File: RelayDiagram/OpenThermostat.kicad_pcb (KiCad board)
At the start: 2 copper layers, 88 parts, among them J1 Conn_01x08_Female, J2 Conn_01x15_Female, J3 Conn_01x15_Female, J4 Conn_01x09_Female, Q1 Q_NMOS_DGS, Q10 Q_NMOS_DGS, Q11 Q_NMOS_DGS, Q12 Q_NMOS_DGS, Q2 Q_NMOS_DGS, Q3 Q_NMOS_DGS, Q4 Q_NMOS_DGS, Q5 Q_NMOS_DGS, Q6 Q_NMOS_DGS, Q7 Q_NMOS_DGS, Q8 Q_NMOS_DGS, Q9 Q_NMOS_DGS, SW2 SW_Push, SW3 SW_Push, SW4 SW_Push, SW5 SW_Push, SW6 SW_Push, U1 PCF8574, U2 LCD, U3 DHT11, U4 EE2-3TNU-L_DPDT_Relay, U5 EE2-3TNU-L_DPDT_Relay, U6 EE2-3TNU-L_DPDT_Relay, U7 EE2-3TNU-L_DPDT_Relay, U8 EE2-3TNU-L_DPDT_Relay, U9 EE2-3TNU-L_DPDT_Relay

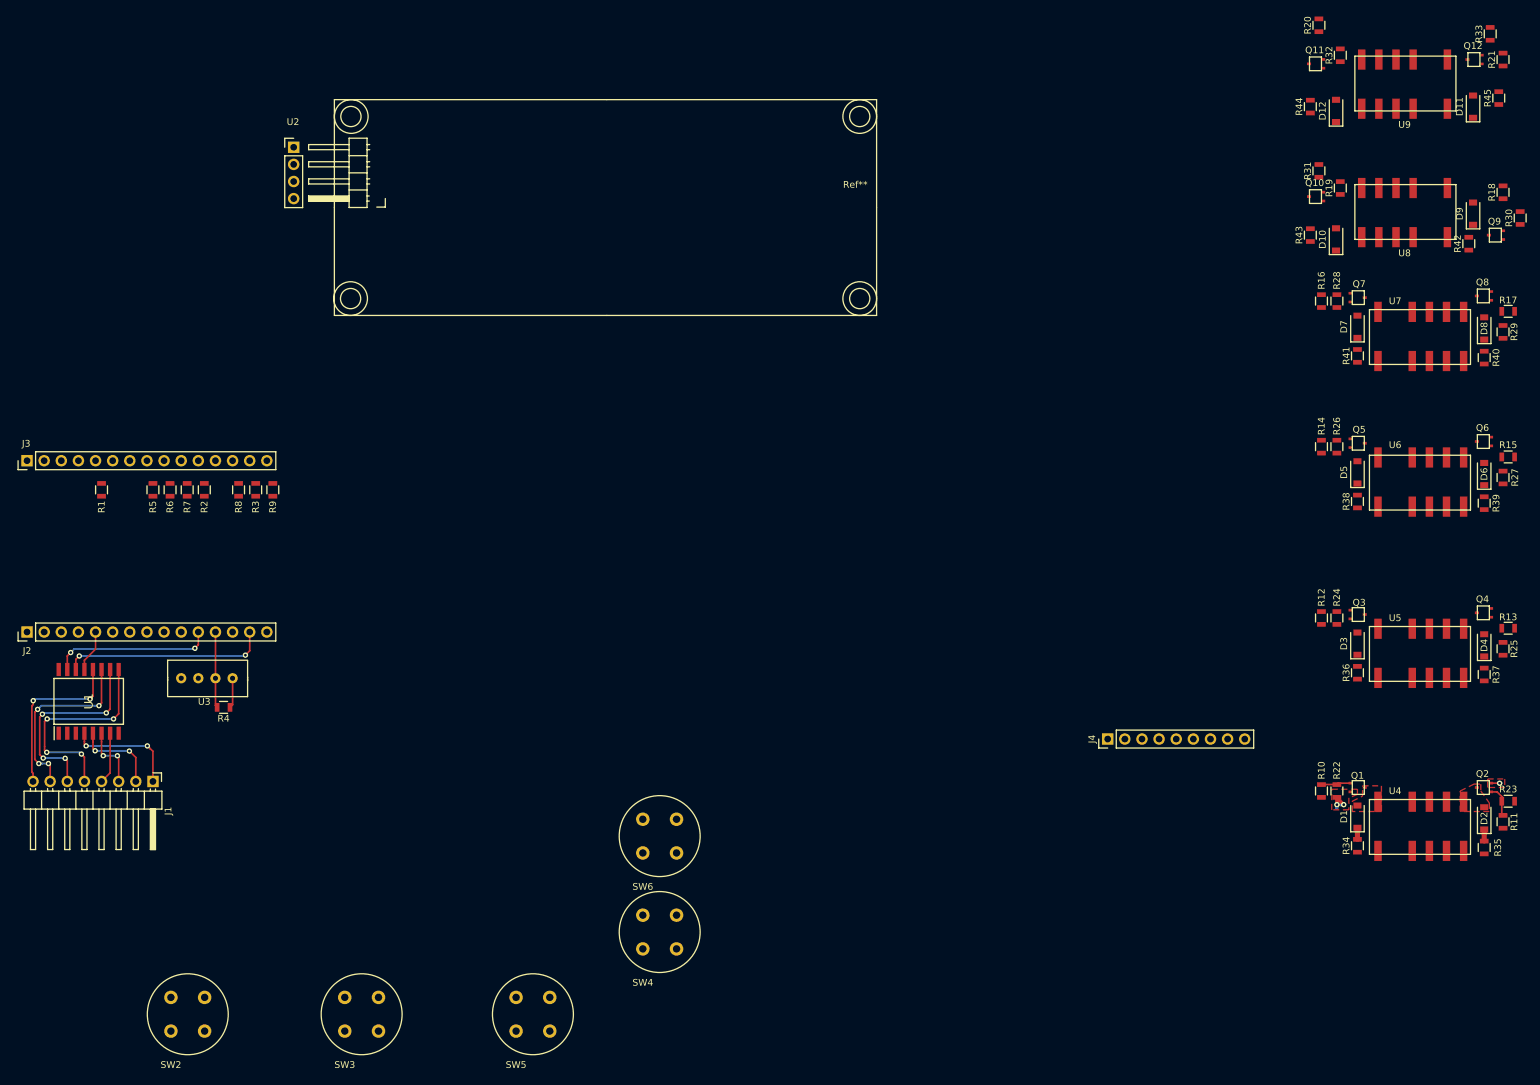
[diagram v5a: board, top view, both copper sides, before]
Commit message: Routed LCD and placed buttons. Added edges to board, but it will most likely need to be extended to route the relays
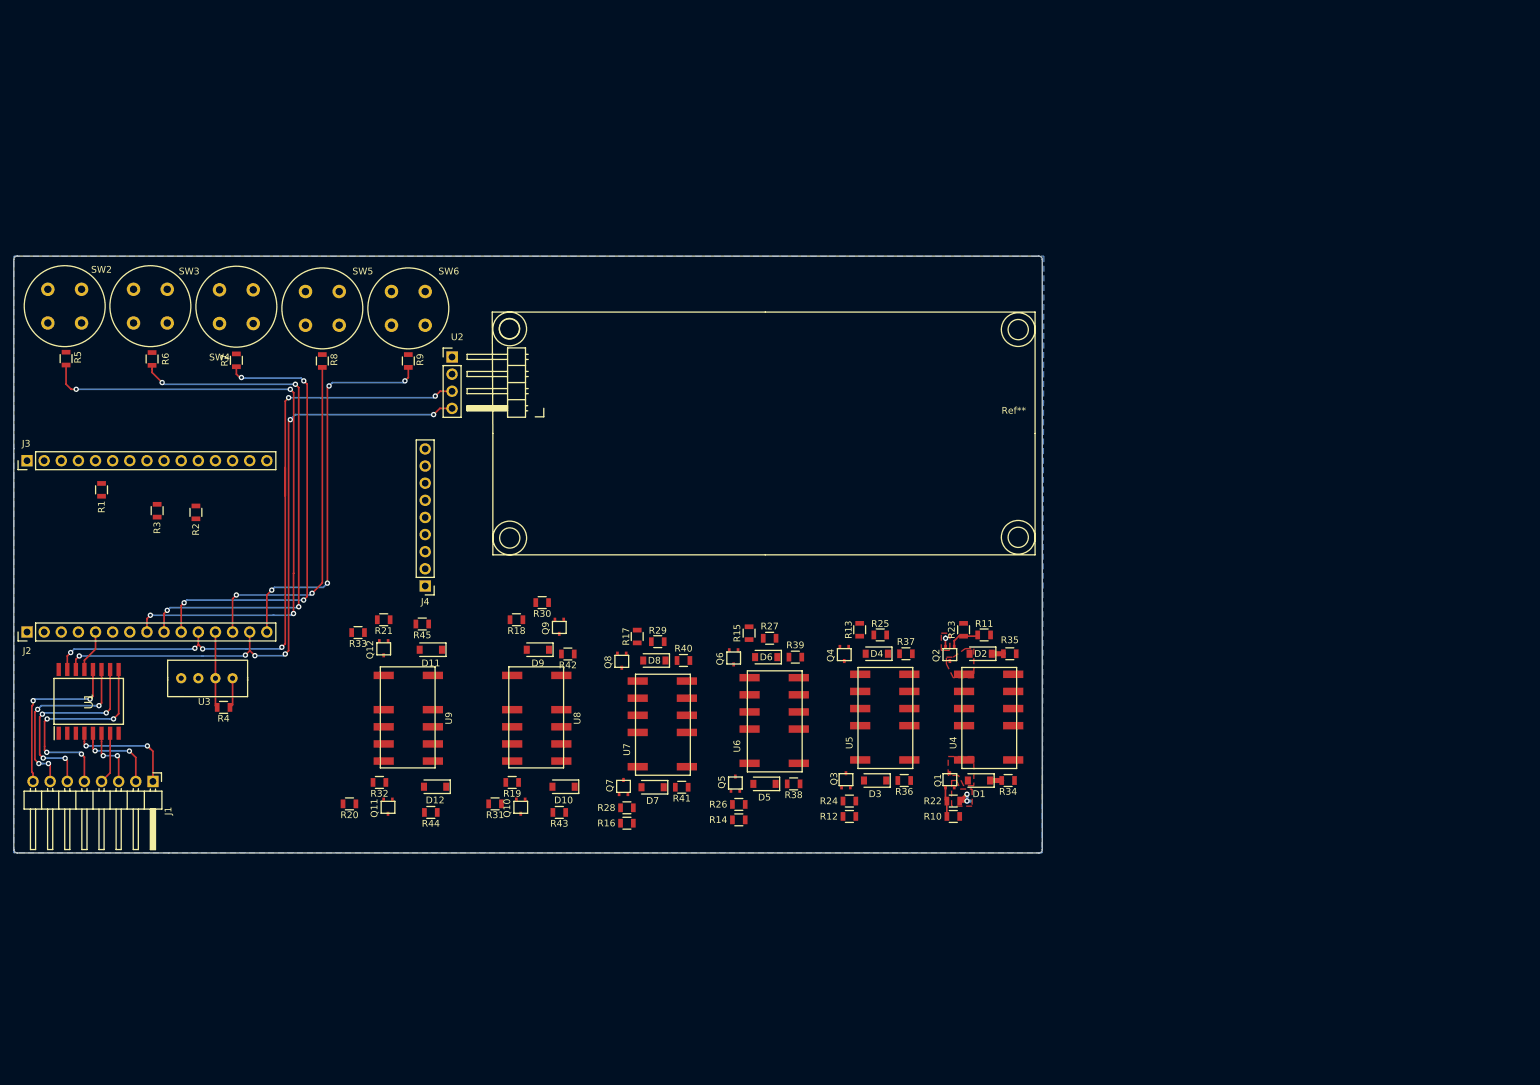
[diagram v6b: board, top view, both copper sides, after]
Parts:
- moved R33 189.9 mm to (102.0, 126.3), turned to 180 degrees
- moved R21 185.6 mm to (105.9, 124.4), turned to 180 degrees
- moved R20 184.4 mm to (100.8, 151.7), turned to 180 degrees
- moved Q12 184.2 mm to (105.9, 127.6), turned to 180 degrees
- moved U9 182.3 mm to (105.9, 132.7), turned to 270 degrees
- moved R32 178.7 mm to (105.2, 148.5), turned to 180 degrees
- moved R45 177.7 mm to (111.6, 125.1), turned to 180 degrees
- moved Q11 176.4 mm to (106.5, 151.1), turned to 180 degrees
- moved D11 174.3 mm to (112.8, 128.9), turned to 180 degrees
- moved R44 167.2 mm to (112.8, 153.0), turned to 180 degrees
- moved D12 167.0 mm to (113.5, 149.2), turned to 180 degrees
- moved R18 159.4 mm to (125.5, 124.4), turned to 180 degrees
- moved U8 156.4 mm to (124.9, 132.7), turned to 270 degrees
- moved R30 155.8 mm to (129.3, 121.9), turned to 180 degrees
- moved R31 154.1 mm to (122.4, 151.7), turned to 180 degrees
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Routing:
- net Net-(J2-Pad8): track 0.00 -> 93.9 mm, vias 0 -> 4
- net Net-(J2-Pad9): track 0.00 -> 79.4 mm, vias 0 -> 4
- net Net-(J2-Pad11): track 24.0 -> 103.1 mm, vias 2 -> 6
- net Net-(J2-Pad10): track 0.00 -> 66.8 mm, vias 0 -> 4
- net Net-(J2-Pad14): track 30.6 -> 96.3 mm, vias 2 -> 6
- net Net-(J2-Pad15): track 0.00 -> 58.3 mm, vias 0 -> 4
- net Net-(J2-Pad13): track 0.00 -> 51.2 mm, vias 0 -> 2
- added copper zone on B.Cu, net GND
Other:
- board outline added: 152.5 x 88.5 mm

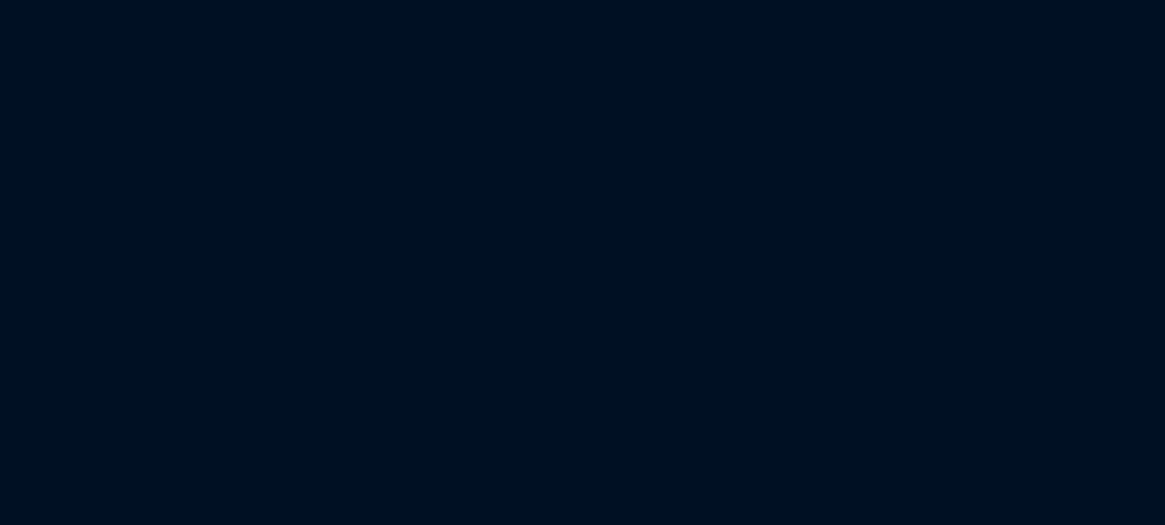
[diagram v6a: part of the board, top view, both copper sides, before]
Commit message: Added Power Components to schematic, Added Footprints
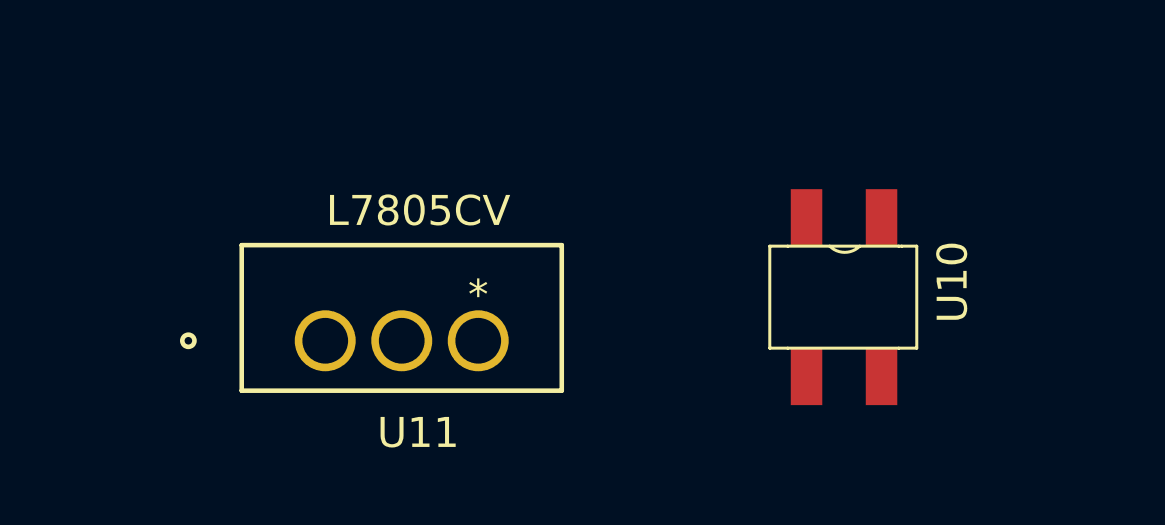
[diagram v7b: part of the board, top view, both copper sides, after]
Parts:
- added U10: MB10S-13, Open_Thermostat:MB10F-13, F.Cu at (137.7, 172.7)
- added U11: L7805CV, Open_Thermostat:L7805CV, F.Cu at (127.2, 169.1)

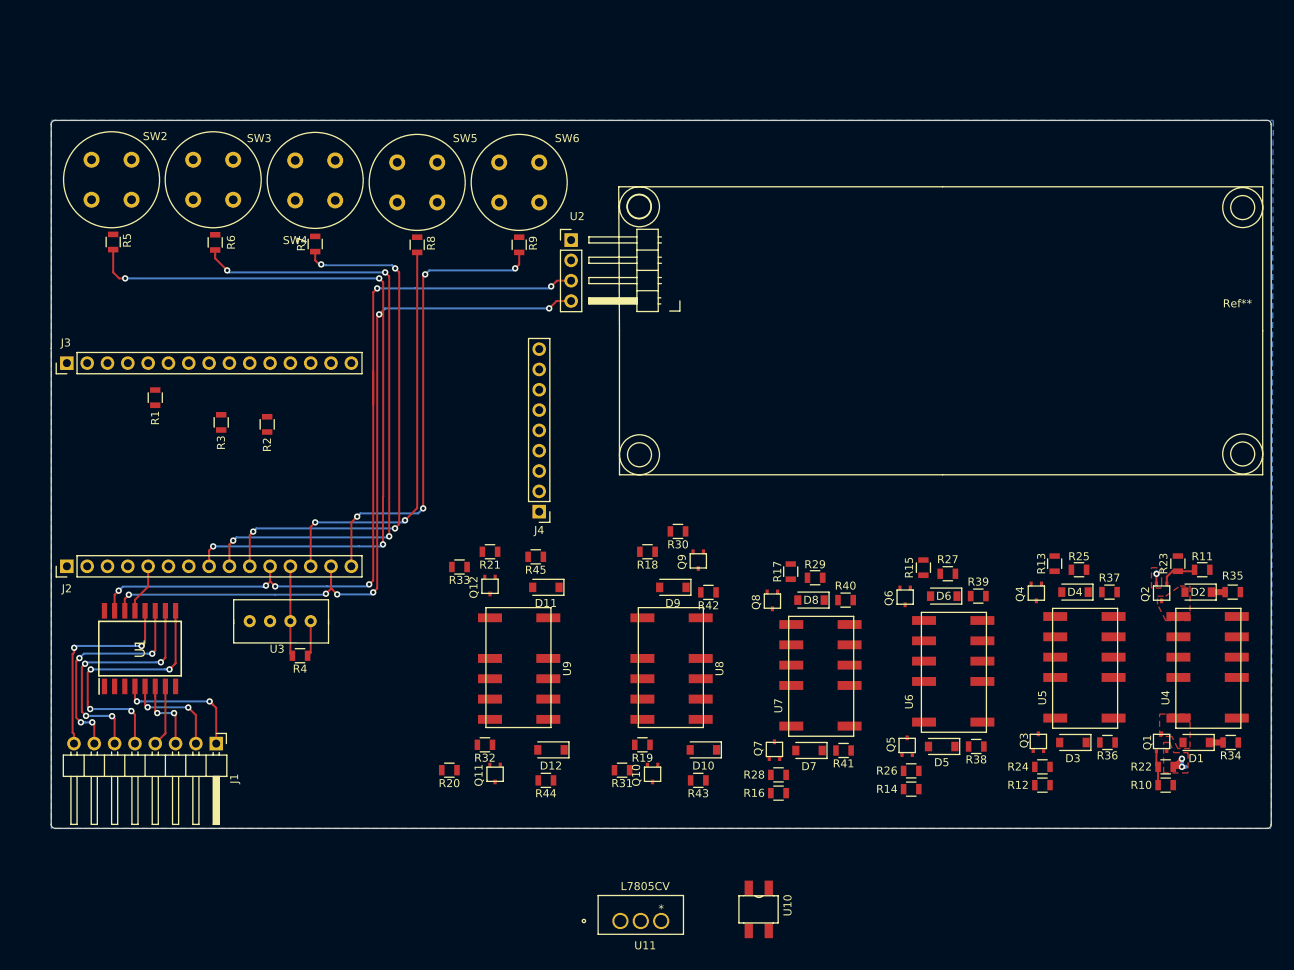
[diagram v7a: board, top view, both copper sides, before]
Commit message: Moved buttons around, changed board size and grounded some components
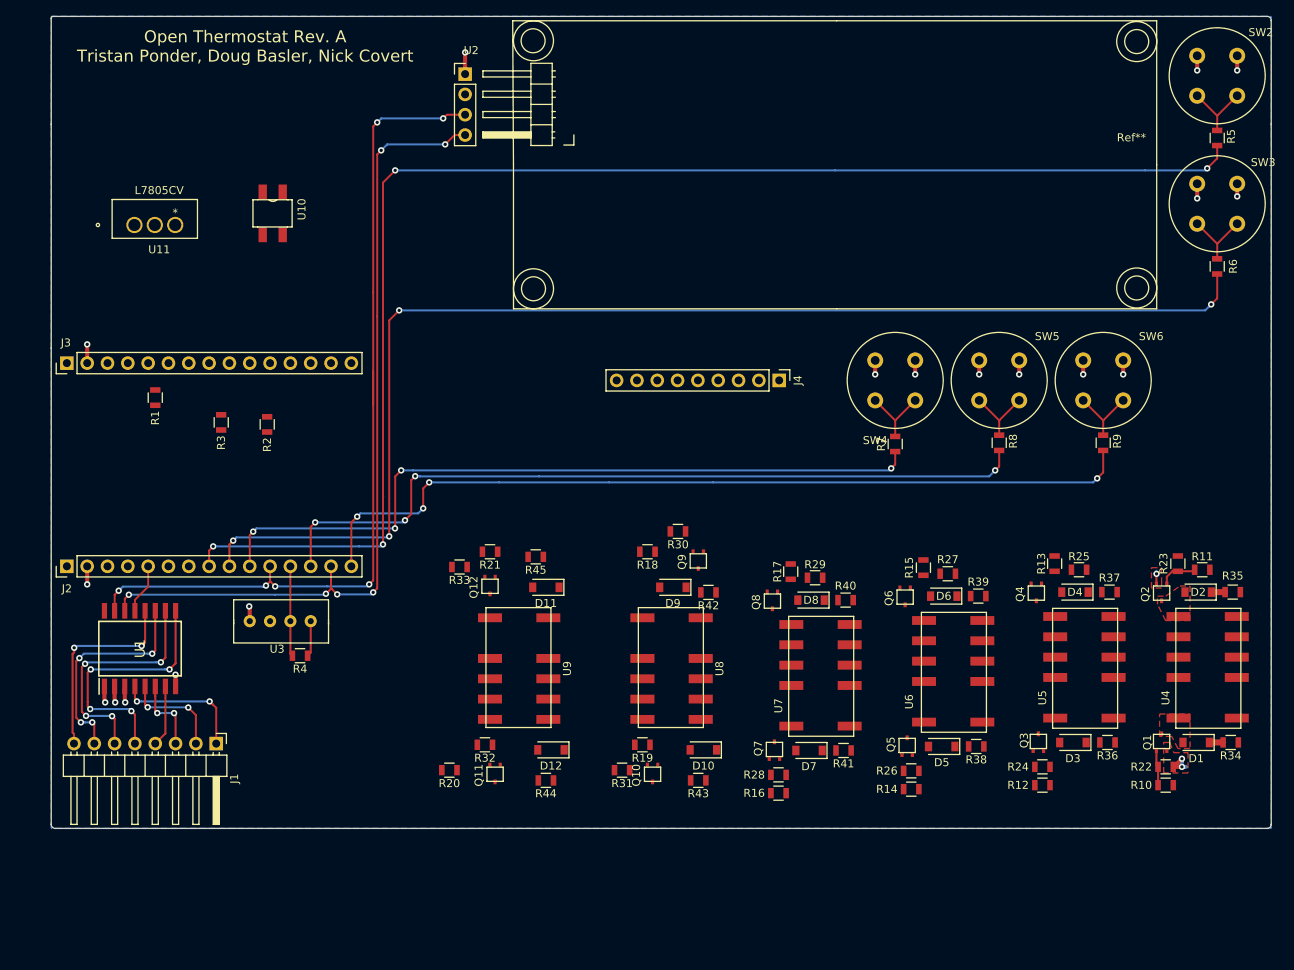
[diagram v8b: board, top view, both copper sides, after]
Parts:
- moved SW2 138.8 mm to (194.2, 67.4)
- moved R5 138.6 mm to (196.8, 72.7)
- moved SW3 125.5 mm to (194.2, 83.4)
- moved R6 125.3 mm to (196.8, 88.8)
- moved U11 106.1 mm to (66.5, 82.1)
- moved U10 106.1 mm to (76.9, 85.7)
- moved R9 77.1 mm to (182.5, 110.8)
- moved SW6 77.1 mm to (180.0, 105.5)
- moved R8 76.8 mm to (169.5, 110.8)
- moved SW5 76.8 mm to (167.0, 105.5)
- moved R7 76.7 mm to (156.5, 111.0)
- moved SW4 76.7 mm to (154.0, 105.5)
- moved J4 34.2 mm to (142.0, 103.0), turned to 270 degrees
- moved Ref** 24.6 mm to (149.2, 76.0)
- moved U2 24.6 mm to (102.7, 64.7)
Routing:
- net Net-(J2-Pad8): track 93.9 -> 176.4 mm
- net Net-(J2-Pad9): track 79.4 -> 157.8 mm
- net Net-(J2-Pad15): track 58.3 -> 106.3 mm
- net Net-(J2-Pad13): track 51.2 -> 98.6 mm, vias 2 -> 4
- net GND: track 5.26 -> 39.6 mm, vias 3 -> 21
- net Net-(J2-Pad10): track 66.8 -> 93.7 mm
- net Net-(R7-Pad2): track 0.00 -> 9.07 mm
- net Net-(R6-Pad2): track 0.00 -> 8.95 mm
- net Net-(R9-Pad2): track 0.00 -> 8.92 mm
- net Net-(R8-Pad2): track 0.00 -> 8.92 mm
- net Net-(R5-Pad2): track 0.00 -> 8.90 mm
- net Net-(J2-Pad11): track 103.1 -> 110.6 mm
- net Net-(J2-Pad14): track 96.3 -> 103.5 mm
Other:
- board size 152.5 x 88.5 mm -> 152.5 x 101.5 mm
- board text added: "Open Thermostat Rev. A Tristan Ponder, Doug Basler, Nick Covert"
